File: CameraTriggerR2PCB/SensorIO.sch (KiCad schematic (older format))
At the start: 17 parts, among them J6 Sensor, J7 Laser, J8 Aux out, J9 HighLowIn, Q3 PN2222A

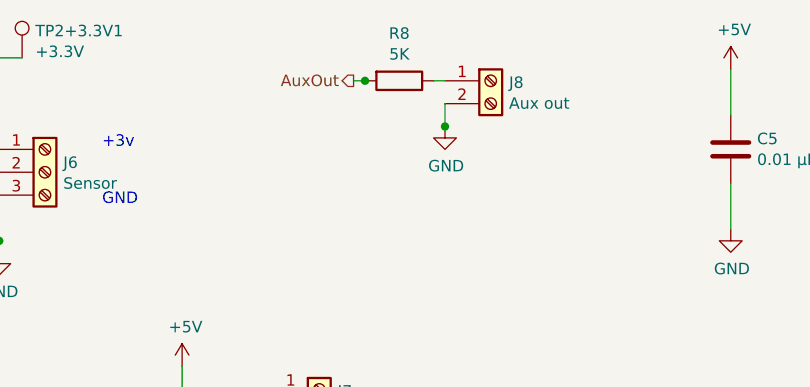
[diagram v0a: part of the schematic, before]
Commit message: Add files via upload
Adding XLR connector
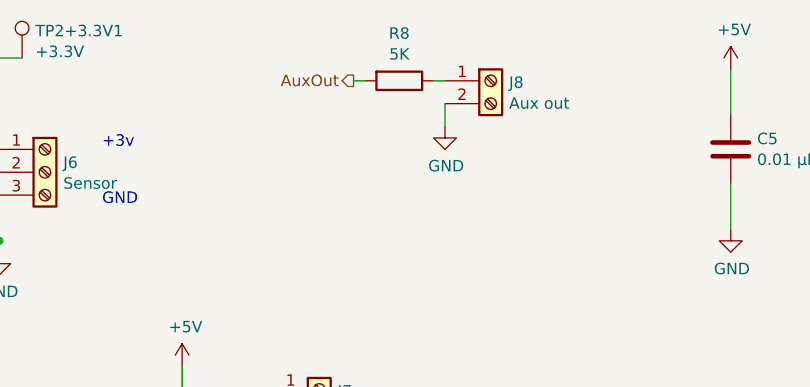
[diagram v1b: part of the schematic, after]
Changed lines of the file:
@@
 $Descr A4 11693 8268
 encoding utf-8
-Sheet 4 8
+Sheet 4 9
 Title ""
 Date ""
@@
 AR Path="/5EBF7D99" Ref="#PWR?"  Part="1"
 AR Path="/5EBF52C3/5EBF7D99" Ref="#PWR023"  Part="1"
+AR Path="/5EBF5198/5EC5B66D/5EBF7D99" Ref="#PWR?"  Part="1"
 F 0 "#PWR023" H 3050 1800 50  0001 C CNN
 F 1 "GND" H 3055 1877 50  0000 C CNN
@@
 AR Path="/5EBF7DA4" Ref="J?"  Part="1"
 AR Path="/5EBF52C3/5EBF7DA4" Ref="J6"  Part="1"
+AR Path="/5EBF5198/5EC5B66D/5EBF7DA4" Ref="J?"  Part="1"
 F 0 "J6" H 3330 1742 50  0000 L CNN
 F 1 "Sensor" H 3330 1651 50  0000 L CNN
@@
 AR Path="/5EBF7DAA" Ref="#PWR?"  Part="1"
 AR Path="/5EBF52C3/5EBF7DAA" Ref="#PWR022"  Part="1"
+AR Path="/5EBF5198/5EC5B66D/5EBF7DAA" Ref="#PWR?"  Part="1"
 F 0 "#PWR022" H 2850 1400 50  0001 C CNN
 F 1 "+3.3V" H 2865 1723 50  0000 C CNN
@@
 AR Path="/5EBF7DB0" Ref="TP2+3.3V?"  Part="1"
 AR Path="/5EBF52C3/5EBF7DB0" Ref="TP2+3.3V1"  Part="1"
+AR Path="/5EBF5198/5EC5B66D/5EBF7DB0" Ref="TP2+3.3V?"  Part="1"
 F 0 "TP2+3.3V1" H 3208 1318 50  0000 L CNN
 F 1 "+3.3V" H 3208 1227 50  0000 L CNN
@@
 AR Path="/5EBF7DBA" Ref="TP?"  Part="1"
 AR Path="/5EBF52C3/5EBF7DBA" Ref="TP1"  Part="1"
+AR Path="/5EBF5198/5EC5B66D/5EBF7DBA" Ref="TP?"  Part="1"
 F 0 "TP1" H 2358 1418 50  0000 L CNN
 F 1 "LowHighIn" H 2358 1327 50  0000 L CNN
@@
 AR Path="/5EBF7DC0" Ref="R?"  Part="1"
 AR Path="/5EBF52C3/5EBF7DC0" Ref="R7"  Part="1"
+AR Path="/5EBF5198/5EC5B66D/5EBF7DC0" Ref="R?"  Part="1"
 F 0 "R7" H 2720 1896 50  0000 L CNN
 F 1 "15K" H 2720 1805 50  0000 L CNN
@@
 AR Path="/5EC068C7" Ref="#PWR?"  Part="1"
 AR Path="/5EBF52C3/5EC068C7" Ref="#PWR026"  Part="1"
+AR Path="/5EBF5198/5EC5B66D/5EC068C7" Ref="#PWR?"  Part="1"
 F 0 "#PWR026" H 5000 1250 50  0001 C CNN
 F 1 "GND" H 5005 1327 50  0000 C CNN
@@
 AR Path="/5EC068CD" Ref="R?"  Part="1"
 AR Path="/5EBF52C3/5EC068CD" Ref="R8"  Part="1"
+AR Path="/5EBF5198/5EC5B66D/5EC068CD" Ref="R?"  Part="1"
 F 0 "R8" V 4593 1300 50  0000 C CNN
 F 1 "5K" V 4684 1300 50  0000 C CNN
@@
 AR Path="/5EC068D4" Ref="J?"  Part="1"
 AR Path="/5EBF52C3/5EC068D4" Ref="J8"  Part="1"
+AR Path="/5EBF5198/5EC5B66D/5EC068D4" Ref="J?"  Part="1"
 F 0 "J8" H 5280 1292 50  0000 L CNN
 F 1 "Aux out" H 5280 1201 50  0000 L CNN
@@
 AR Path="/5EC2BBE6" Ref="J?"  Part="1"
 AR Path="/5EBF52C3/5EC2BBE6" Ref="J7"  Part="1"
+AR Path="/5EBF5198/5EC5B66D/5EC2BBE6" Ref="J?"  Part="1"
 F 0 "J7" H 4530 2642 50  0000 L CNN
 F 1 "Laser" H 4530 2551 50  0000 L CNN
@@
 AR Path="/5EC2BBEC" Ref="D?"  Part="1"
 AR Path="/5EBF52C3/5EC2BBEC" Ref="D5"  Part="1"
+AR Path="/5EBF5198/5EC5B66D/5EC2BBEC" Ref="D?"  Part="1"
 F 0 "D5" H 2693 3166 50  0000 C CNN
 F 1 "LED Arm" H 2693 3075 50  0000 C CNN
@@
 AR Path="/5EC2BBF2" Ref="R?"  Part="1"
 AR Path="/5EBF52C3/5EC2BBF2" Ref="R6"  Part="1"
+AR Path="/5EBF5198/5EC5B66D/5EC2BBF2" Ref="R?"  Part="1"
 F 0 "R6" H 2270 2996 50  0000 L CNN
 F 1 "1K" H 2270 2905 50  0000 L CNN
@@
 AR Path="/5EC2BBF9" Ref="Q?"  Part="1"
 AR Path="/5EBF52C3/5EC2BBF9" Ref="Q3"  Part="1"
+AR Path="/5EBF5198/5EC5B66D/5EC2BBF9" Ref="Q?"  Part="1"
 F 0 "Q3" H 3440 2996 50  0000 L CNN
 F 1 "PN2222A" H 3440 2905 50  0000 L CNN
@@
 AR Path="/5EC2BBFF" Ref="#PWR?"  Part="1"
 AR Path="/5EBF52C3/5EC2BBFF" Ref="#PWR024"  Part="1"
+AR Path="/5EBF5198/5EC5B66D/5EC2BBFF" Ref="#PWR?"  Part="1"
 F 0 "#PWR024" H 3350 3050 50  0001 C CNN
 F 1 "GND" H 3355 3127 50  0000 C CNN
@@
 AR Path="/5EC2BC0B" Ref="#PWR?"  Part="1"
 AR Path="/5EBF52C3/5EC2BC0B" Ref="#PWR025"  Part="1"
+AR Path="/5EBF5198/5EC5B66D/5EC2BC0B" Ref="#PWR?"  Part="1"
 F 0 "#PWR025" H 3850 2400 50  0001 C CNN
 F 1 "+5V" H 3865 2723 50  0000 C CNN
@@
 AR Path="/5EC2BC11" Ref="TP3Arm?"  Part="1"
 AR Path="/5EBF52C3/5EC2BC11" Ref="TP3Arm1"  Part="1"
+AR Path="/5EBF5198/5EC5B66D/5EC2BC11" Ref="TP3Arm?"  Part="1"
 F 0 "TP3Arm1" H 2108 2768 50  0000 L CNN
 F 1 "Arm" H 2108 2677 50  0000 L CNN
@@
 AR Path="/5EC71B67" Ref="C?"  Part="1"
 AR Path="/5EBF52C3/5EC71B67" Ref="C4"  Part="1"
+AR Path="/5EBF5198/5EC5B66D/5EC71B67" Ref="C?"  Part="1"
 F 0 "C4" H 2915 4796 50  0000 L CNN
 F 1 "0.01 μF" H 2915 4705 50  0000 L CNN
@@
 AR Path="/5EC71B6D" Ref="C?"  Part="1"
 AR Path="/5EBF52C3/5EC71B6D" Ref="C3"  Part="1"
+AR Path="/5EBF5198/5EC5B66D/5EC71B6D" Ref="C?"  Part="1"
 F 0 "C3" H 2465 4796 50  0000 L CNN
 F 1 "0.01 μF" H 2465 4705 50  0000 L CNN
@@
 AR Path="/5EC71B73" Ref="#PWR?"  Part="1"
 AR Path="/5EBF52C3/5EC71B73" Ref="#PWR021"  Part="1"
+AR Path="/5EBF5198/5EC5B66D/5EC71B73" Ref="#PWR?"  Part="1"
 F 0 "#PWR021" H 2800 4750 50  0001 C CNN
 F 1 "GND" H 2805 4827 50  0000 C CNN
@@
 AR Path="/5EC71B79" Ref="#PWR?"  Part="1"
 AR Path="/5EBF52C3/5EC71B79" Ref="#PWR020"  Part="1"
+AR Path="/5EBF5198/5EC5B66D/5EC71B79" Ref="#PWR?"  Part="1"
 F 0 "#PWR020" H 2350 4850 50  0001 C CNN
 F 1 "GND" H 2355 4927 50  0000 C CNN
@@
 AR Path="/5EC7B62C" Ref="C?"  Part="1"
 AR Path="/5EBF52C3/5EC7B62C" Ref="C6"  Part="1"
+AR Path="/5EBF5198/5EC5B66D/5EC7B62C" Ref="C?"  Part="1"
 F 0 "C6" H 6815 1646 50  0000 L CNN
 F 1 "0.01 μF" H 6815 1555 50  0000 L CNN
@@
 AR Path="/5EC7B632" Ref="C?"  Part="1"
 AR Path="/5EBF52C3/5EC7B632" Ref="C5"  Part="1"
+AR Path="/5EBF5198/5EC5B66D/5EC7B632" Ref="C?"  Part="1"
 F 0 "C5" H 6365 1646 50  0000 L CNN
 F 1 "0.01 μF" H 6365 1555 50  0000 L CNN
@@
 AR Path="/5EC7B638" Ref="#PWR?"  Part="1"
 AR Path="/5EBF52C3/5EC7B638" Ref="#PWR032"  Part="1"
+AR Path="/5EBF5198/5EC5B66D/5EC7B638" Ref="#PWR?"  Part="1"
 F 0 "#PWR032" H 6700 1600 50  0001 C CNN
 F 1 "GND" H 6705 1677 50  0000 C CNN
@@
 AR Path="/5EC7B63E" Ref="#PWR?"  Part="1"
 AR Path="/5EBF52C3/5EC7B63E" Ref="#PWR030"  Part="1"
+AR Path="/5EBF5198/5EC5B66D/5EC7B63E" Ref="#PWR?"  Part="1"
 F 0 "#PWR030" H 6250 1700 50  0001 C CNN
 F 1 "GND" H 6255 1777 50  0000 C CNN
@@
 AR Path="/5EC7B646" Ref="#PWR?"  Part="1"
 AR Path="/5EBF52C3/5EC7B646" Ref="#PWR031"  Part="1"
+AR Path="/5EBF5198/5EC5B66D/5EC7B646" Ref="#PWR?"  Part="1"
 F 0 "#PWR031" H 6700 1100 50  0001 C CNN
 F 1 "+3.3V" H 6715 1423 50  0000 C CNN
@@
 AR Path="/5EC7B64C" Ref="#PWR?"  Part="1"
 AR Path="/5EBF52C3/5EC7B64C" Ref="#PWR029"  Part="1"
+AR Path="/5EBF5198/5EC5B66D/5EC7B64C" Ref="#PWR?"  Part="1"
 F 0 "#PWR029" H 6250 1100 50  0001 C CNN
 F 1 "+5V" H 6265 1423 50  0000 C CNN
@@
 AR Path="/5EC89FF6" Ref="#PWR?"  Part="1"
 AR Path="/5EBF52C3/5EC89FF6" Ref="#PWR027"  Part="1"
+AR Path="/5EBF5198/5EC5B66D/5EC89FF6" Ref="#PWR?"  Part="1"
 F 0 "#PWR027" H 6050 4050 50  0001 C CNN
 F 1 "GND" H 6055 4127 50  0000 C CNN
@@
 AR Path="/5EC89FFE" Ref="J?"  Part="1"
 AR Path="/5EBF52C3/5EC89FFE" Ref="J9"  Part="1"
+AR Path="/5EBF5198/5EC5B66D/5EC89FFE" Ref="J?"  Part="1"
 F 0 "J9" H 5668 3775 50  0000 C CNN
 F 1 "HighLowIn" H 5668 3866 50  0000 C CNN
@@
 AR Path="/5EC8A004" Ref="#PWR?"  Part="1"
 AR Path="/5EBF52C3/5EC8A004" Ref="#PWR028"  Part="1"
+AR Path="/5EBF5198/5EC5B66D/5EC8A004" Ref="#PWR?"  Part="1"
 F 0 "#PWR028" H 6100 3850 50  0001 C CNN
 F 1 "+3.3V" H 6115 4173 50  0000 C CNN
@@
 AR Path="/5EC914A2" Ref="TP?"  Part="1"
 AR Path="/5EBF52C3/5EC914A2" Ref="TP2"  Part="1"
+AR Path="/5EBF5198/5EC5B66D/5EC914A2" Ref="TP?"  Part="1"
 F 0 "TP2" H 6558 3768 50  0000 L CNN
 F 1 "HighLowIn" H 6558 3677 50  0000 L CNN
@@
 Text HLabel 2200 4350 0    50   Input ~ 0
 AuxIn
-Connection ~ 5000 1500
-Connection ~ 4650 1300
 $EndSCHEMATC
